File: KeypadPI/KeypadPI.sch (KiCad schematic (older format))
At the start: 55 parts, among them J1 Conn_01x04, J2 Conn_02x20_Odd_Even, J3 Conn_01x01, J4 Conn_01x01, J5 Conn_01x01, J6 Conn_01x01, J7 Conn_01x04, Q1 2N7000, Q2 2N7000, SW1 SW_Push, SW10 SW_Push, SW11 SW_Push, SW12 SW_Push, SW13 SW_Push, SW14 SW_Push, SW15 SW_Push, SW16 SW_Push, SW2 SW_Push, SW3 SW_Push, SW4 SW_Push, SW5 SW_Push, SW6 SW_Push, SW7 SW_Push, SW8 SW_Push, SW9 SW_Push, U1 74HC595

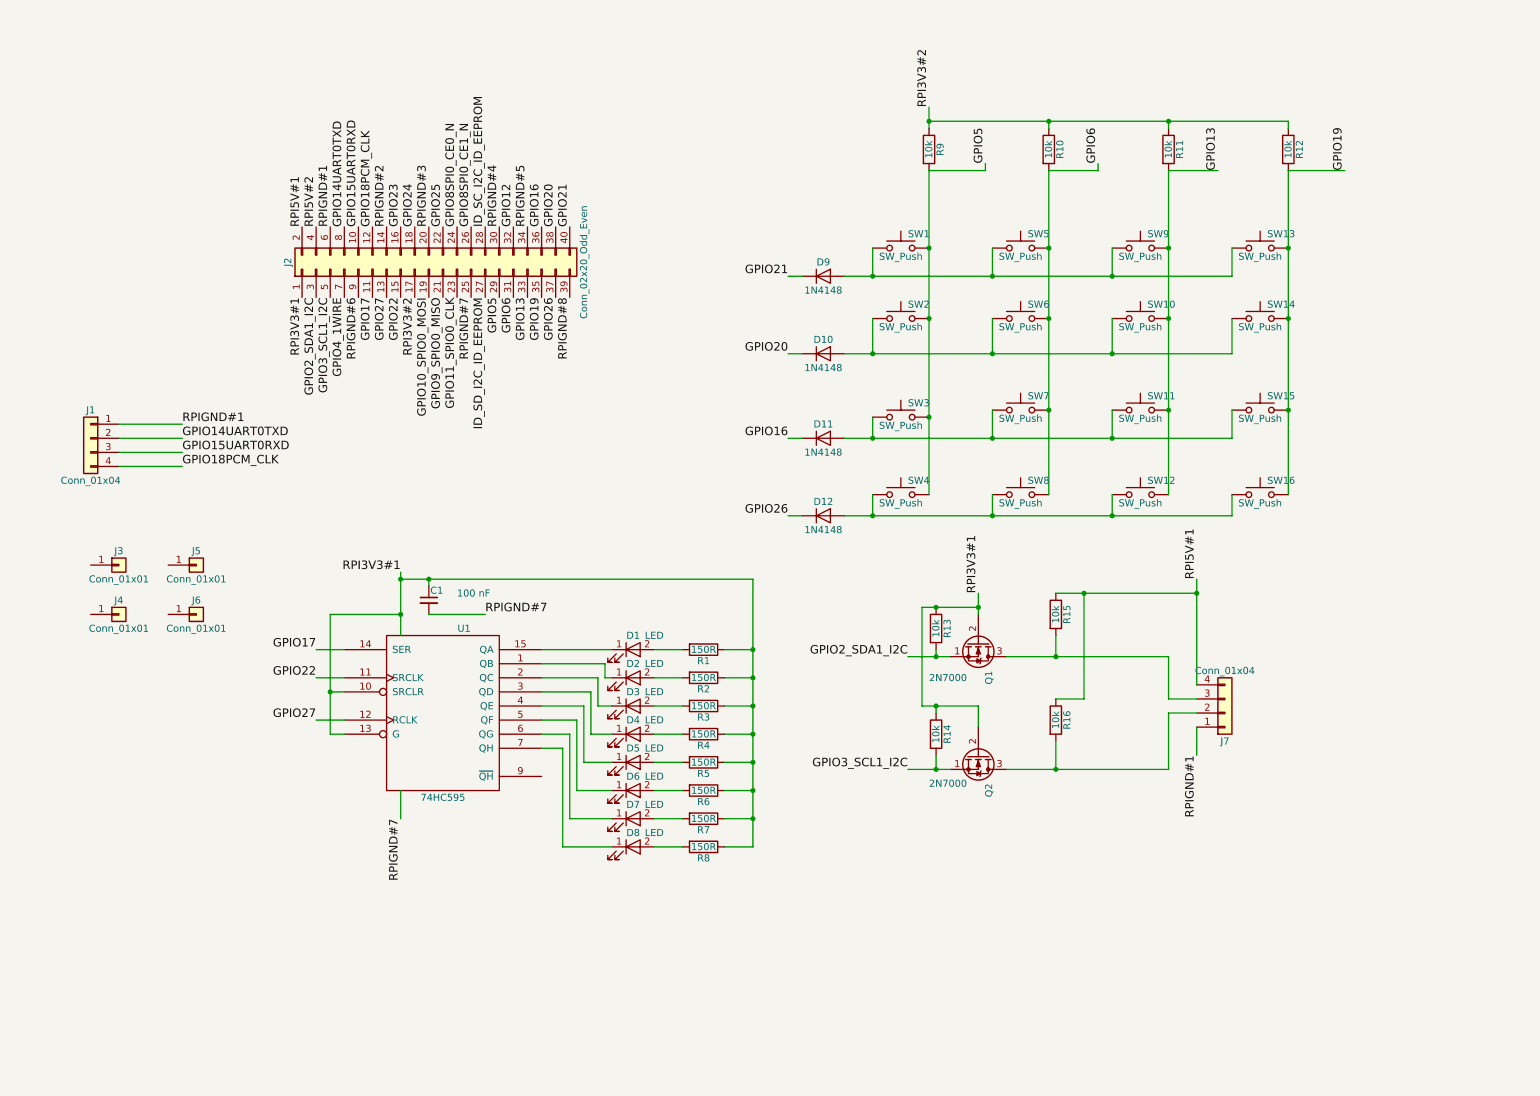
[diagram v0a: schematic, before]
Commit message: Added audio input and output to keypad PCB
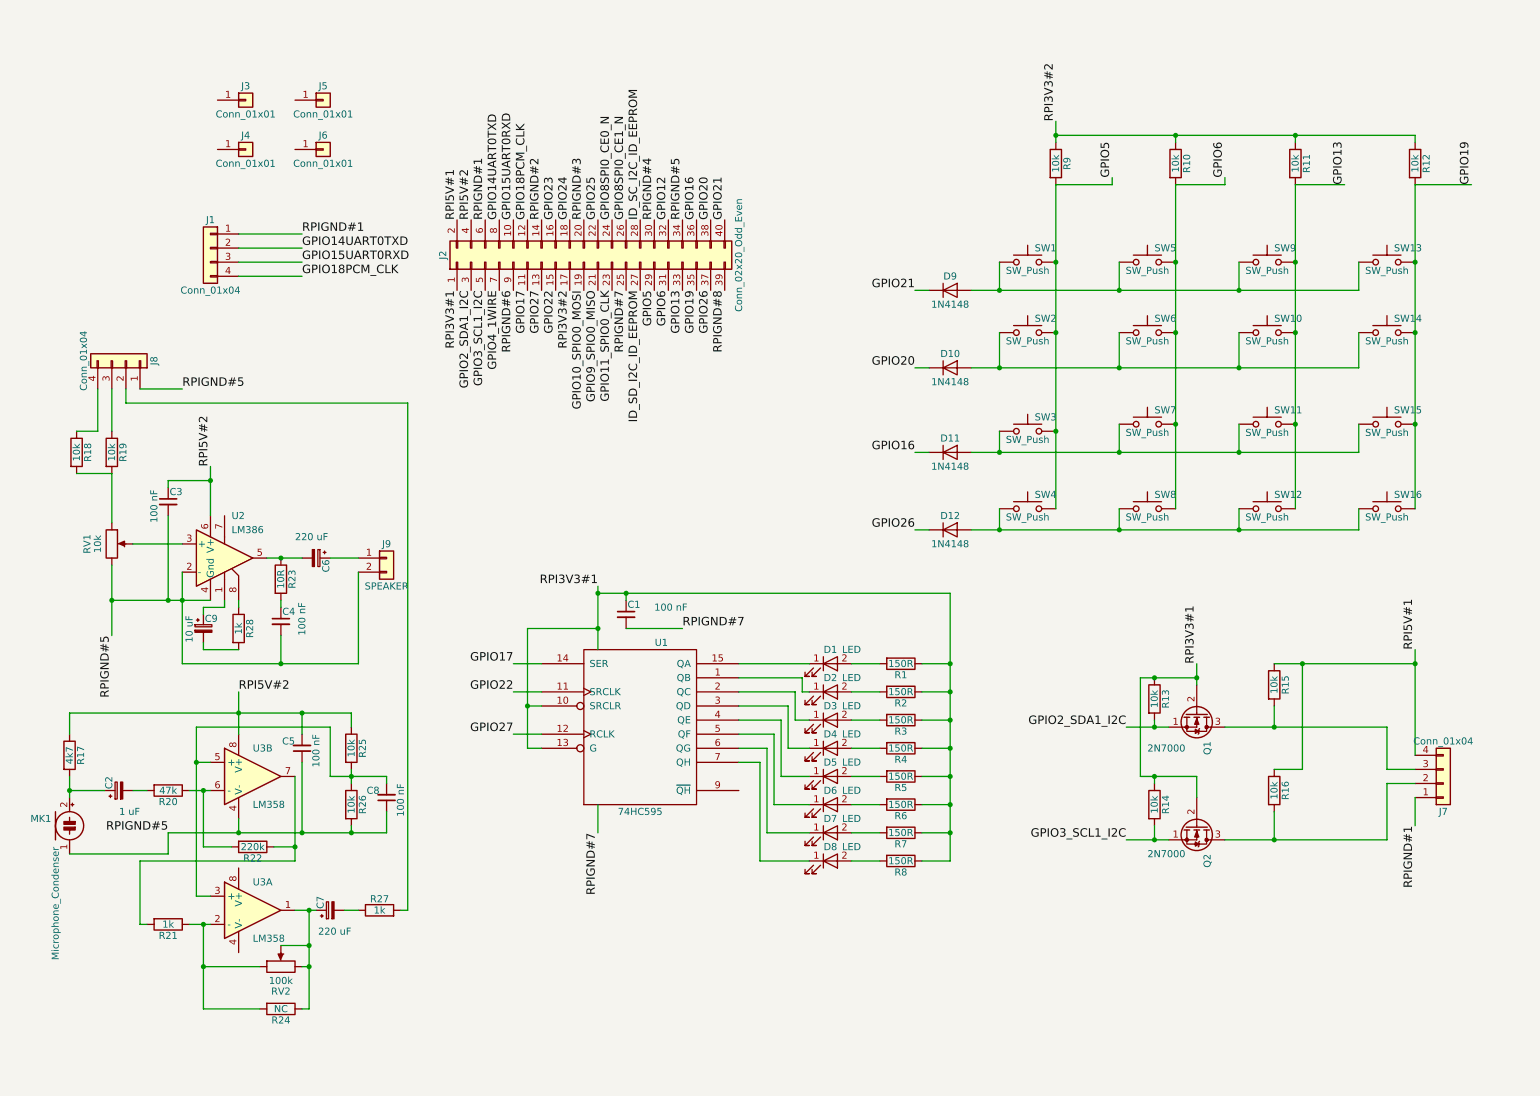
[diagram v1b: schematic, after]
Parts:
- added C2: 1 uF, Capacitors_THT:CP_Radial_D5.0mm_P2.50mm, symbol CP_Small
- added C3, C4, C5, C8: 100 nF, Capacitors_THT:C_Disc_D5.0mm_W2.5mm_P2.50mm, symbol C_Small
- added C6, C7: 220 uF, Capacitors_THT:CP_Radial_D5.0mm_P2.50mm, symbol CP_Small
- added C9: 10 uF, Capacitors_THT:CP_Radial_D5.0mm_P2.50mm, symbol CP_Small
- added J8: Conn_01x04, Pin_Headers:Pin_Header_Straight_1x04_Pitch2.54mm, symbol Conn_01x04
- added J9: SPEAKER, Connectors_Terminal_Blocks:TerminalBlock_bornier-2_P5.08mm, symbol Conn_01x02
- added MK1: Microphone_Condenser, KeypadPI:CondenserMic, symbol Microphone_Condenser
- added R17: 4k7, Resistors_THT:R_Axial_DIN0207_L6.3mm_D2.5mm_P7.62mm_Horizontal, symbol R
- added R18, R19, R25, R26: 10k, Resistors_THT:R_Axial_DIN0207_L6.3mm_D2.5mm_P7.62mm_Horizontal, symbol R
- added R20: 47k, Resistors_THT:R_Axial_DIN0207_L6.3mm_D2.5mm_P7.62mm_Horizontal, symbol R
- added R21, R27, R28: 1k, Resistors_THT:R_Axial_DIN0207_L6.3mm_D2.5mm_P7.62mm_Horizontal, symbol R
- added R22: 220k, Resistors_THT:R_Axial_DIN0207_L6.3mm_D2.5mm_P7.62mm_Horizontal, symbol R
- added R23: 10R, Resistors_THT:R_Axial_DIN0207_L6.3mm_D2.5mm_P7.62mm_Horizontal, symbol R
- added R24: NC, Resistors_THT:R_Axial_DIN0207_L6.3mm_D2.5mm_P7.62mm_Horizontal, symbol R
- added RV1: 10k, Potentiometers:Potentiometer_Trimmer_Bourns_3296W, symbol POT
- added RV2: 100k, Potentiometers:Potentiometer_Trimmer_Bourns_3296W, symbol POT
- added U2: LM386, Housings_DIP:DIP-8_W7.62mm_Socket, symbol LM386
- added U3: LM358, Housings_DIP:DIP-8_W7.62mm_Socket, symbol LM358
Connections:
- net RPI5V#2: now also C3.1, C5.2, R17.1, R25.1, U2.6 (V+), U3.8 (V+)
- net RPIGND#5: now also C3.2, C4.2, C5.1, C8.1, J8.1 (Pin_1), J9.2 (Pin_2), MK1.1 (-), R26.2, RV1.3, U2.2 (-), U2.4 (Gnd), U3.4 (V-)
- new net: C9.1, U2.1
- new net: RV1.2, U2.3 (+)
- new net: C6.2, R23.1, U2.5
- new net: R28.1, U2.8
- new net: R18.2, R19.2, RV1.1
- new net: J8.2 (Pin_2), R27.2
- new net: J8.3 (Pin_3), R19.1
- new net: J8.4 (Pin_4), R18.1
- new net: C4.1, R23.2
- new net: C6.1, J9.1 (Pin_1)
- new net: C8.2, R25.2, R26.1, U3.3 (+), U3.5 (+)
- new net: R20.1, R22.2, U3.6 (-)
- new net: R21.2, R22.1, U3.7
- new net: C7.1, R24.1, RV2.2, RV2.3, U3.1
- new net: R21.1, R24.2, RV2.1, U3.2 (-)
- new net: C7.2, R27.1
- new net: C2.2, R20.2
- new net: C2.1, MK1.2 (+), R17.2
- new net: C9.2, R28.2
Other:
- moved on the sheet: C1, D1, D10, D11, D12, D2, D3, D4, D5, D6, D7, D8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

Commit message: Added second microphone to keypad
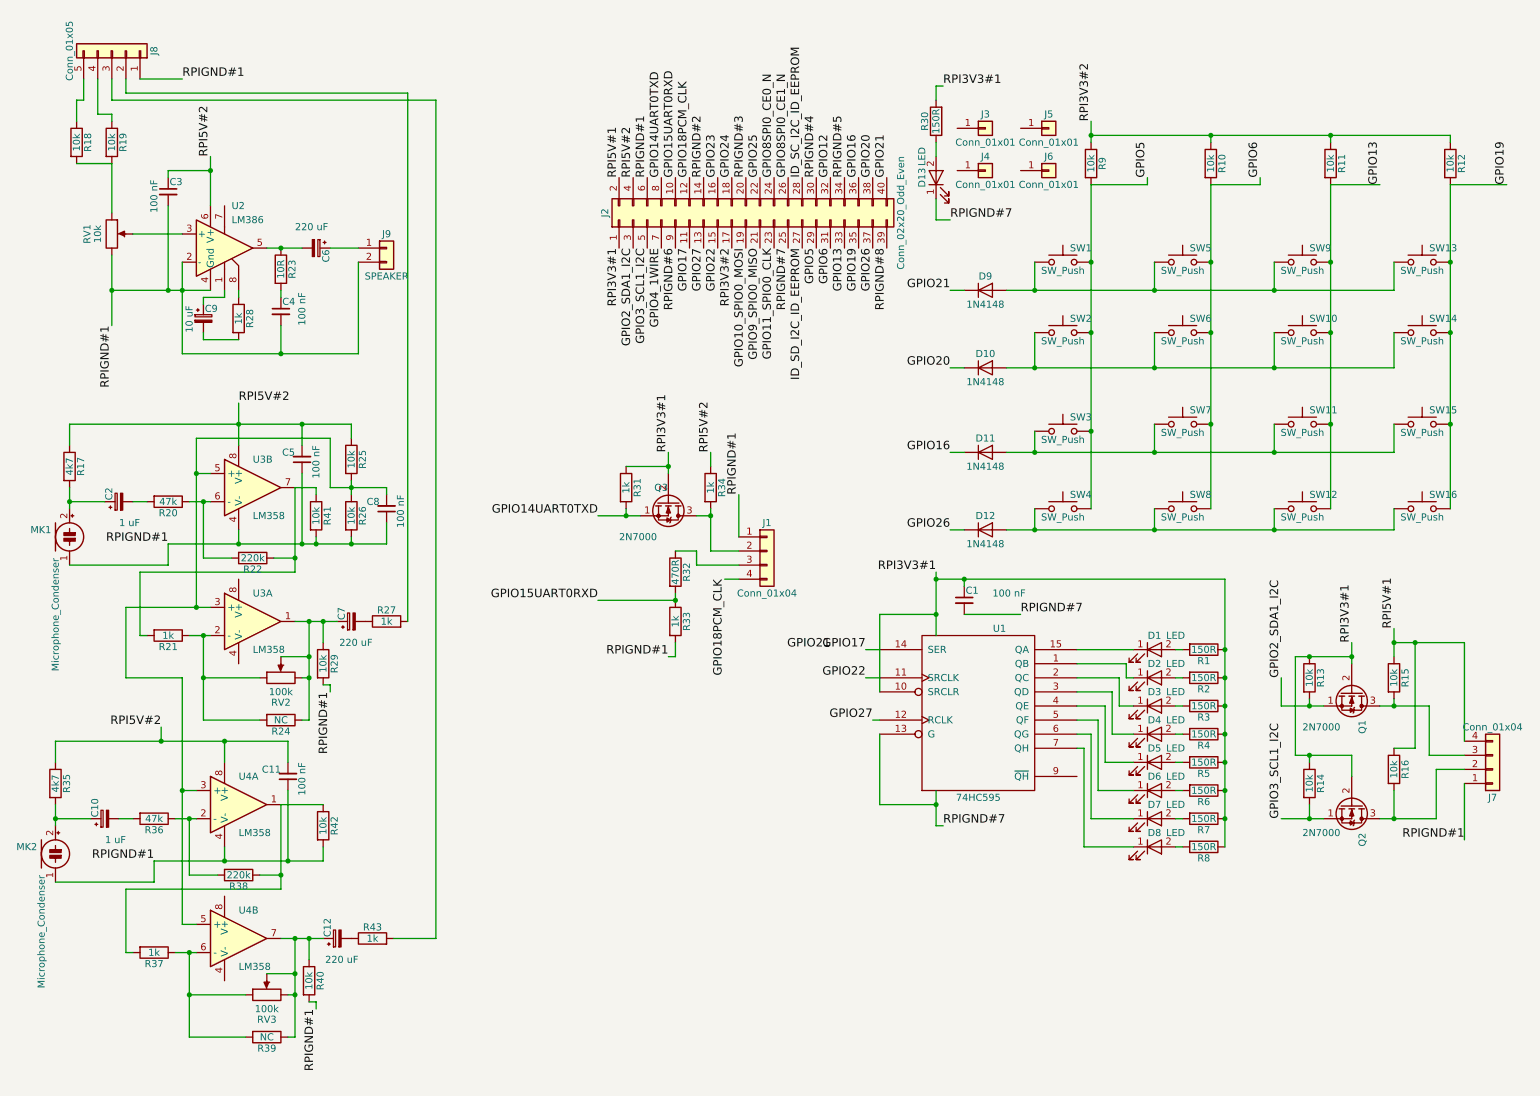
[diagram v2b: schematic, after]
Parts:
- removed J8: Conn_01x04, Pin_Headers:Pin_Header_Straight_1x04_Pitch2.54mm, symbol Conn_01x04
- added C10: 1 uF, Capacitors_THT:CP_Radial_D5.0mm_P2.50mm, symbol CP_Small
- added C11: 100 nF, Capacitors_THT:C_Disc_D5.0mm_W2.5mm_P2.50mm, symbol C_Small
- added C12: 220 uF, Capacitors_THT:CP_Radial_D5.0mm_P2.50mm, symbol CP_Small
- added D13: LED, LEDs:LED_D5.0mm, symbol LED
- added J8: Conn_01x05, Pin_Headers:Pin_Header_Straight_1x05_Pitch2.54mm, symbol Conn_01x05
- added MK2: Microphone_Condenser, KeypadPI:CondenserMic, symbol Microphone_Condenser
- added Q3: 2N7000, TO_SOT_Packages_THT:TO-92_Inline_Wide, symbol 2N7000
- added R29, R40, R41, R42: 10k, Resistors_THT:R_Axial_DIN0207_L6.3mm_D2.5mm_P7.62mm_Horizontal, symbol R
- added R30: 150R, Resistors_THT:R_Axial_DIN0207_L6.3mm_D2.5mm_P7.62mm_Horizontal, symbol R
- added R31, R33, R34, R37, R43: 1k, Resistors_THT:R_Axial_DIN0207_L6.3mm_D2.5mm_P7.62mm_Horizontal, symbol R
- added R32: 470R, Resistors_THT:R_Axial_DIN0207_L6.3mm_D2.5mm_P7.62mm_Horizontal, symbol R
- added R35: 4k7, Resistors_THT:R_Axial_DIN0207_L6.3mm_D2.5mm_P7.62mm_Horizontal, symbol R
- added R36: 47k, Resistors_THT:R_Axial_DIN0207_L6.3mm_D2.5mm_P7.62mm_Horizontal, symbol R
- added R38: 220k, Resistors_THT:R_Axial_DIN0207_L6.3mm_D2.5mm_P7.62mm_Horizontal, symbol R
- added R39: NC, Resistors_THT:R_Axial_DIN0207_L6.3mm_D2.5mm_P7.62mm_Horizontal, symbol R
- added RV3: 100k, Potentiometers:Potentiometer_Trimmer_Bourns_3296W, symbol POT
- added U4: LM358, Housings_DIP:DIP-8_W7.62mm_Socket, symbol LM358
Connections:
- net GND: now also U1.13 (G), D13.1 (K)
- net GPIO14UART0TXD: now also Q3.1 (S), R31.2; no longer J1.2 (Pin_2)
- net GPIO15UART0RXD: now also R32.2, R33.1; no longer J1.3 (Pin_3)
- net RPI5V#2: now also C11.2, R34.1, R35.1, U4.8 (V+)
- net RPIGND#1: now also C3.2, C4.2, C5.1, C8.1, J9.2 (Pin_2), MK1.1 (-), R26.2, RV1.3, U2.2 (-), U2.4 (Gnd), U3.4 (V-), C11.1, J8.1 (Pin_1), MK2.1 (-), R29.2, R33.2, R40.2, R41.2, R42.2, U4.4 (V-)
- net RPIGND#5: no longer C3.2, C4.2, C5.1, C8.1, J9.2 (Pin_2), MK1.1 (-), R26.2, RV1.3, U2.2 (-), U2.4 (Gnd), U3.4 (V-)
- net VCC: now also Q3.2 (G), R30.2, R31.1; no longer U1.13 (G)
- net at R27.2: now also J8.2 (Pin_2)
- net at R19.1: now also J8.4 (Pin_4)
- net at R18.1: now also J8.5 (Pin_5)
- net at C8.2, R25.2, R26.1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: now also U4.3 (+), U4.5 (+)
- net at R21.2, R22.1, U3.7: now also R41.1
- net at C7.1, R24.1, RV2.2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: now also R29.1
- new net: J1.2 (Pin_2), Q3.3 (D), R34.2
- new net: J1.3 (Pin_3), R32.1
- new net: D13.2 (A), R30.1
- new net: R37.2, R38.1, R42.1, U4.1
- new net: R36.1, R38.2, U4.2 (-)
- new net: R37.1, R39.2, RV3.1, U4.6 (-)
- new net: C12.1, R39.1, R40.1, RV3.2, RV3.3, U4.7
- new net: C12.2, R43.1
- new net: C10.2, R36.2
- new net: J8.3 (Pin_3), R43.2
- new net: C10.1, MK2.2 (+), R35.2
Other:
- moved on the sheet: C1, C2, C3, C4, C5, C6, C7, C8, C9, D1, D10, D11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

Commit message: A few fixes
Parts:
- added R44: NC, Resistors_THT:R_Axial_DIN0207_L6.3mm_D2.5mm_P7.62mm_Horizontal, symbol R
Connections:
- net GPIO15UART0RXD: now also R44.1
- net VCC: now also R44.2

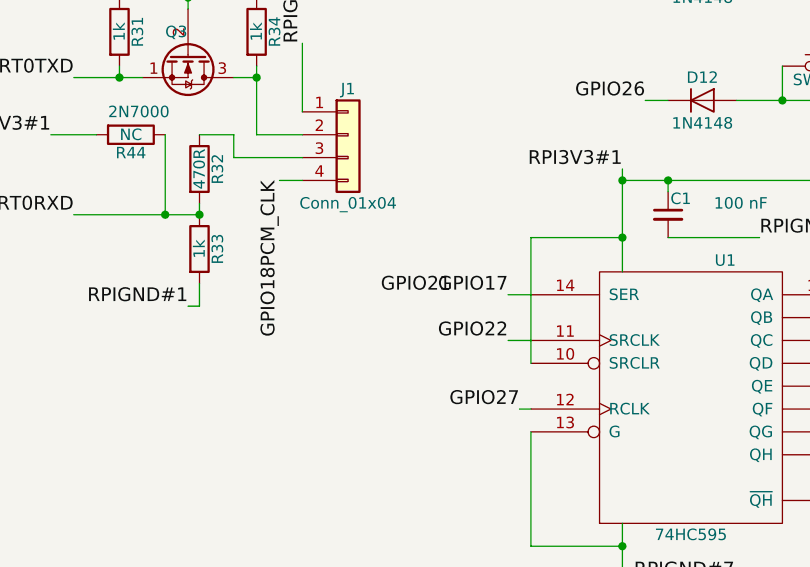
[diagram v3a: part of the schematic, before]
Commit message: Begin code for controlling robot with command line
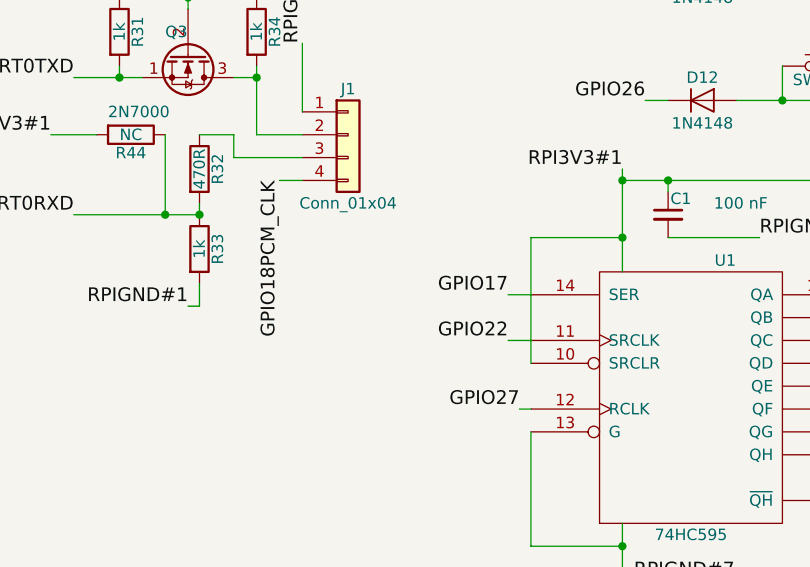
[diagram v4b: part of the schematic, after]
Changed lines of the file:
@@
 Text Label 7200 2850 2    60   ~ 0
 GPIO20
-Text Label 6350 4850 2    60   ~ 0
-GPIO21
 Text Label 7200 4000 2    60   ~ 0
 GPIO26
